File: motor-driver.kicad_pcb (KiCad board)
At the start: 4 copper layers, 35 x 27 mm, 108 parts, among them J2 SIGNAL, J3 PWR, J4 RTMI, Q4 SIZ322DT, Q5 SIZ322DT, Q6 SIZ322DT, U1 TMC4671, U2 74LVC3G17, U3 74LVC3G17, U4 TMC6200

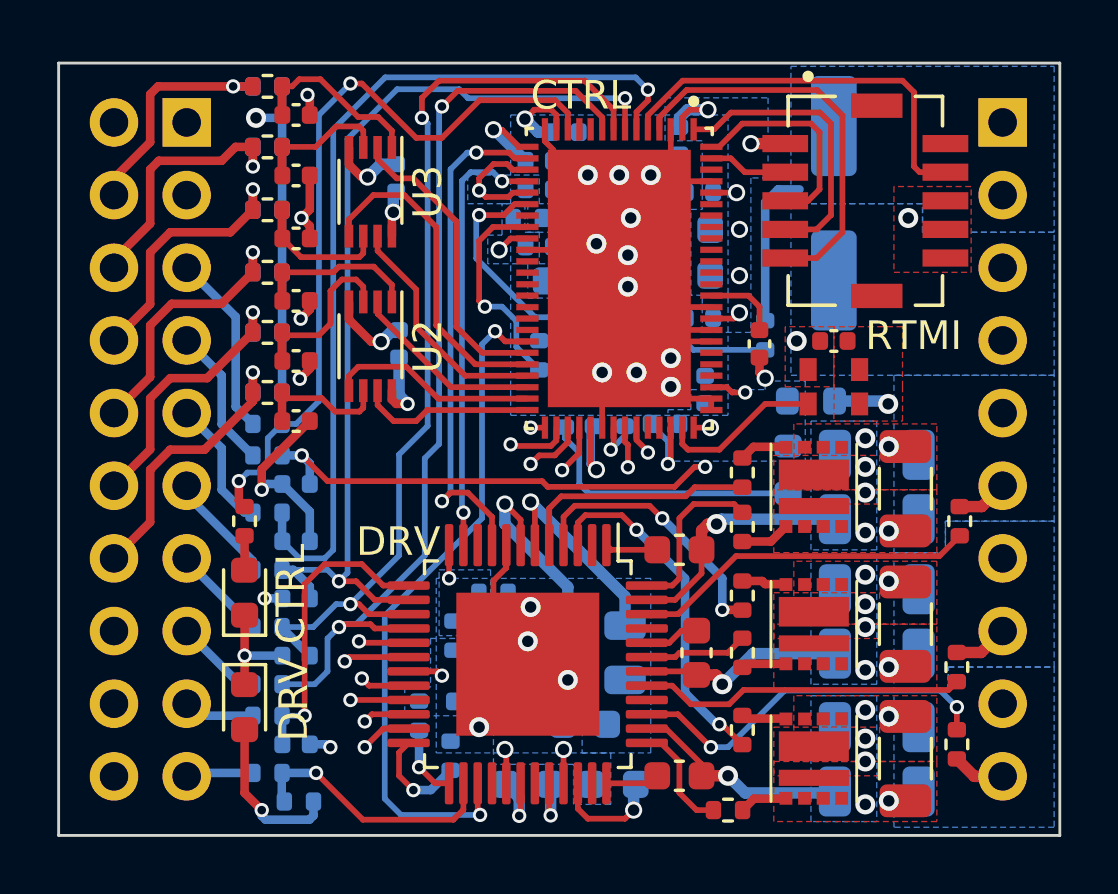
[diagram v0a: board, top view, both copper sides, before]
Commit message: Applied the fixes to the pcb.
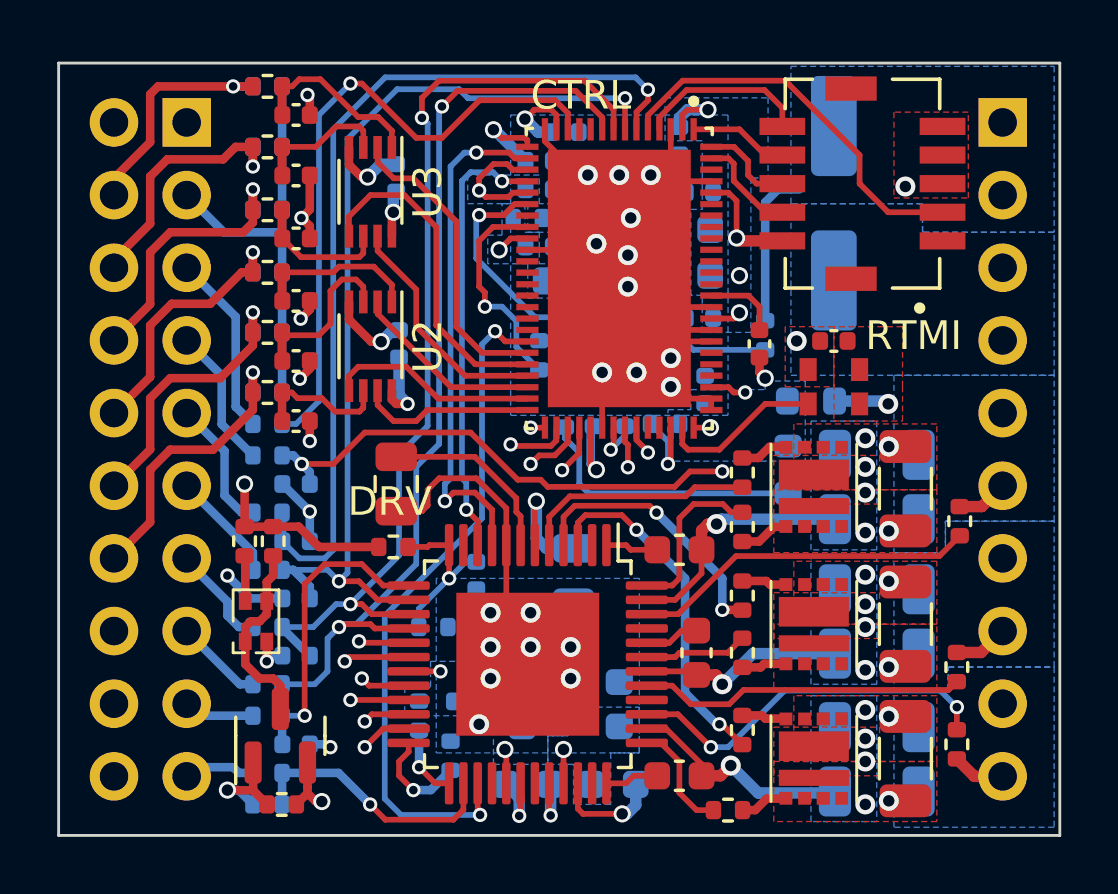
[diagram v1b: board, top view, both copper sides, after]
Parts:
- removed D2: BLUE, LED_SMD:LED_0603_1608Metric
- added Q1: BSS138, Package_TO_SOT_SMD:SOT-23, F.Cu at (130.7, 99.8)
- added R49: 100, Resistor_SMD:R_0402_1005Metric, B.Cu at (130.2, 102.2)
- added R50: 10K, Resistor_SMD:R_0402_1005Metric, F.Cu at (130.7, 102.2)
- added R51: 1, Resistor_SMD:R_0402_1005Metric, B.Cu at (140.8, 99.3)
- C25: moved to F.Cu
- C34: value 47uF, 63V -> 47uF, 35V
- C37, C38, C39: value 2.2uF, 100V -> 2.2uF, 50V
- D1: value RED -> B2972USNB05; footprint LED_SMD:LED_0603_1608Metric -> B2972USNB05:B2972USNB05
- R15: value 1.5K, %1 -> 4.7K, %1; moved to F.Cu
- R30, R31, R32, R33, R34, R35: value 22, %1 -> 10, %1
- R36, R37, R38, R39, R40, R41: value 0.033, %1, 1W -> 0.005, %1, 1W
- R47: value 220, %1 -> 330; moved to F.Cu
- R48: value 100, %1 -> 330
- moved R47 9.30 mm to (129.4, 93.0), turned to 90 degrees
- moved C25 8.41 mm to (134.7, 91.0)
- moved R15 3.74 mm to (134.6, 93.2), turned to 180 degrees
- moved C24 3.24 mm to (140.9, 94.2)
- moved D1 3.03 mm to (129.8, 95.8), turned to 90 degrees
- moved R16 2.42 mm to (136.0, 96.0)
- moved C32 1.71 mm to (137.5, 94.2), turned to 90 degrees
- moved C28 1.39 mm to (142.5, 98.7), turned to -90 degrees
- moved R48 1.22 mm to (130.4, 93.0), turned to 90 degrees
- moved J4 0.61 mm to (151.0, 80.5), turned to 180 degrees
- moved C23 0.36 mm to (139.1, 98.7)
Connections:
- C27 pad 2: +24V -> Net-(U4-VS)
- C28 pad 2: +24V -> Net-(U4-VS)
- D1 pad 2: Net-(D1-A) -> Net-(D1-A1)
- J2 pad 1: +5V -> +3.3V
- J2 pad 3: +3.3V -> +5V
- R15 pad 2: +3.3V -> +5V
- R47 pad 1: /DRV_FAULT -> Net-(D1-A2)
- R47 pad 2: Net-(D1-A) -> +5V
- R48 pad 1: /CTRL_STATUS -> Net-(D1-A1)
- R48 pad 2: Net-(D2-A) -> +5V
- U1 pad 18: /CUR_W -> /CUR_V
- U4 pad 10: /Driver/CUR_V -> /CUR_V
- U4 pad 11: /CUR_W -> /Driver/CUR_W
- U4 pad 33: +24V -> Net-(U4-VS)
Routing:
- net /CUR_V: track 0.00 -> 15.5 mm, vias 0 -> 2
- net /CUR_W: track 15.3 -> 0.00 mm, vias 2 -> 0
- net +5V: track 12.8 -> 22.2 mm
- net /DBG_SPI_MISO: track 14.0 -> 6.02 mm
- net /DBG_SPI_MOSI: track 10.2 -> 3.47 mm
- net Net-(D1-A1): track 0.00 -> 6.72 mm
- net Net-(D1-A): track 5.68 -> 0.00 mm, vias 1 -> 0
- net GND: track 32.2 -> 37.1 mm, vias 34 -> 40
- net Net-(U4-VOFS/TEST): track 1.16 -> 5.96 mm
- net /DBG_SPI_SCK: track 7.34 -> 3.31 mm
- net /CTRL_STATUS: track 26.7 -> 22.9 mm, vias 2 -> 1
- net Net-(Q1-G): track 0.00 -> 3.67 mm, vias 0 -> 1
- net Net-(U4-12VOUT): track 7.26 -> 4.30 mm
- net +3.3V: track 18.1 -> 19.9 mm, vias 12 -> 10
- net Net-(D1-A2): track 0.00 -> 1.60 mm
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- added copper zone on B.Cu, net Net-(U4-VS)
- removed copper zone on B.Cu, net Net-(U4-VOFS/TEST)
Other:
- board text added: "V.2023.0.2"
- board text removed: "V.2023.0.1"

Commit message: Change the mosfets to SIZ342ADT.
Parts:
- Q4, Q5, Q6: value SIZ322DT -> SIZ342ADT
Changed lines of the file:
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@@
     (descr "PowerPAIR® 3 x 3")
     (tags "MOSFET (N-Channel)")
-    (property "MPN" "SIZ322DT-T1-GE3")
+    (property "MPN" "SIZ342ADT-T1-GE3")
     (property "Sheetfile" "driver.kicad_sch")
     (property "Sheetname" "Driver")
@@
         (effects (font (size 1 1) (thickness 0.15)))
     )
-    (fp_text value "SIZ322DT" (at 0 0) (layer "F.SilkS") hide
+    (fp_text value "SIZ342ADT" (at 0 0) (layer "F.SilkS") hide
         (effects (font (size 1.27 1.27) (thickness 0.254)))
     )
@@
     (descr "PowerPAIR® 3 x 3")
     (tags "MOSFET (N-Channel)")
-    (property "MPN" "SIZ322DT-T1-GE3")
+    (property "MPN" "SIZ342ADT-T1-GE3")
     (property "Sheetfile" "driver.kicad_sch")
     (property "Sheetname" "Driver")
@@
         (effects (font (size 1 1) (thickness 0.15)))
     )
-    (fp_text value "SIZ322DT" (at 0 0) (layer "F.SilkS") hide
+    (fp_text value "SIZ342ADT" (at 0 0) (layer "F.SilkS") hide
         (effects (font (size 1.27 1.27) (thickness 0.254)))
     )
@@
     (descr "PowerPAIR® 3 x 3")
     (tags "MOSFET (N-Channel)")
-    (property "MPN" "SIZ322DT-T1-GE3")
+    (property "MPN" "SIZ342ADT-T1-GE3")
     (property "Sheetfile" "driver.kicad_sch")
     (property "Sheetname" "Driver")
@@
         (effects (font (size 1 1) (thickness 0.15)))
     )
-    (fp_text value "SIZ322DT" (at 0 0) (layer "F.SilkS") hide
+    (fp_text value "SIZ342ADT" (at 0 0) (layer "F.SilkS") hide
         (effects (font (size 1.27 1.27) (thickness 0.254)))
     )

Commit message: Small improvements.
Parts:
- added TP1: EN TestPoint, TestPoint:TestPoint_Pad_D1.0mm, B.Cu at (138.7, 92.5)
- C23, C27, C28: value 100nF, 100V -> 100nF, 50V; footprint Capacitor_SMD:C_0603_1608Metric -> Capacitor_SMD:C_0402_1005Metric
- C26: value 22nF, 100V -> 22nF, 50V; footprint Capacitor_SMD:C_0603_1608Metric -> Capacitor_SMD:C_0402_1005Metric
- C37, C38, C39: footprint Capacitor_SMD:C_1206_3216Metric -> Capacitor_SMD:C_0805_2012Metric
- D1: value B2972USNB05 -> 1.6(L)X0.8(W)X0.5(H) MM RED/BLUE
- moved R43 0.41 mm to (154.2, 97.0)
- moved C26 0.28 mm to (139.5, 101.7)
- moved C27 0.22 mm to (142.2, 101.7)
- moved R42 0.20 mm to (154.2, 92.3)
- moved C37 0.20 mm to (152.7, 91.2)
- moved C38 0.20 mm to (152.7, 95.9)
- moved C39 0.20 mm to (152.7, 100.6)
- moved R44 0.10 mm to (154.2, 100.1)
- moved C28 0.10 mm to (142.5, 98.8)
- moved D1 0.10 mm to (129.8, 95.7)
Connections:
- J2 pad 10: /HALL_UX -> /HALL_V
- J2 pad 12: /HALL_V -> /HALL_WY
- J2 pad 14: /HALL_WY -> GND
- J2 pad 2: unconnected-(J2-Pin_2-Pad2) -> /ENC_A
- J2 pad 4: /ENC_A -> /ENC_B
- J2 pad 6: /ENC_B -> /ENC_C
- J2 pad 8: /ENC_C -> /HALL_UX
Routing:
- net /ENC_C: track 9.50 -> 7.12 mm
- net /HALL_WY: track 10.1 -> 7.96 mm
- net /HALL_UX: track 9.35 -> 7.24 mm
- net /HALL_V: track 9.80 -> 7.69 mm
- net /ENC_B: track 8.83 -> 6.92 mm
- net /ENC_A: track 7.86 -> 6.07 mm
- net /Controller/DRV_EN: track 23.9 -> 25.0 mm
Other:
- board text added: "+"
- board text added: "-"
- board text added: "Ali Salehi"
- board text added: "U"
- board text added: "V"
- board text added: "W"
